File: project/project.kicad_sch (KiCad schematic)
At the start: 26 parts, among them J1 FFC Connector, U1 PCA9555PW, U2 74HC165, U3 ISO1540, U4 GX101, U5 74HC165

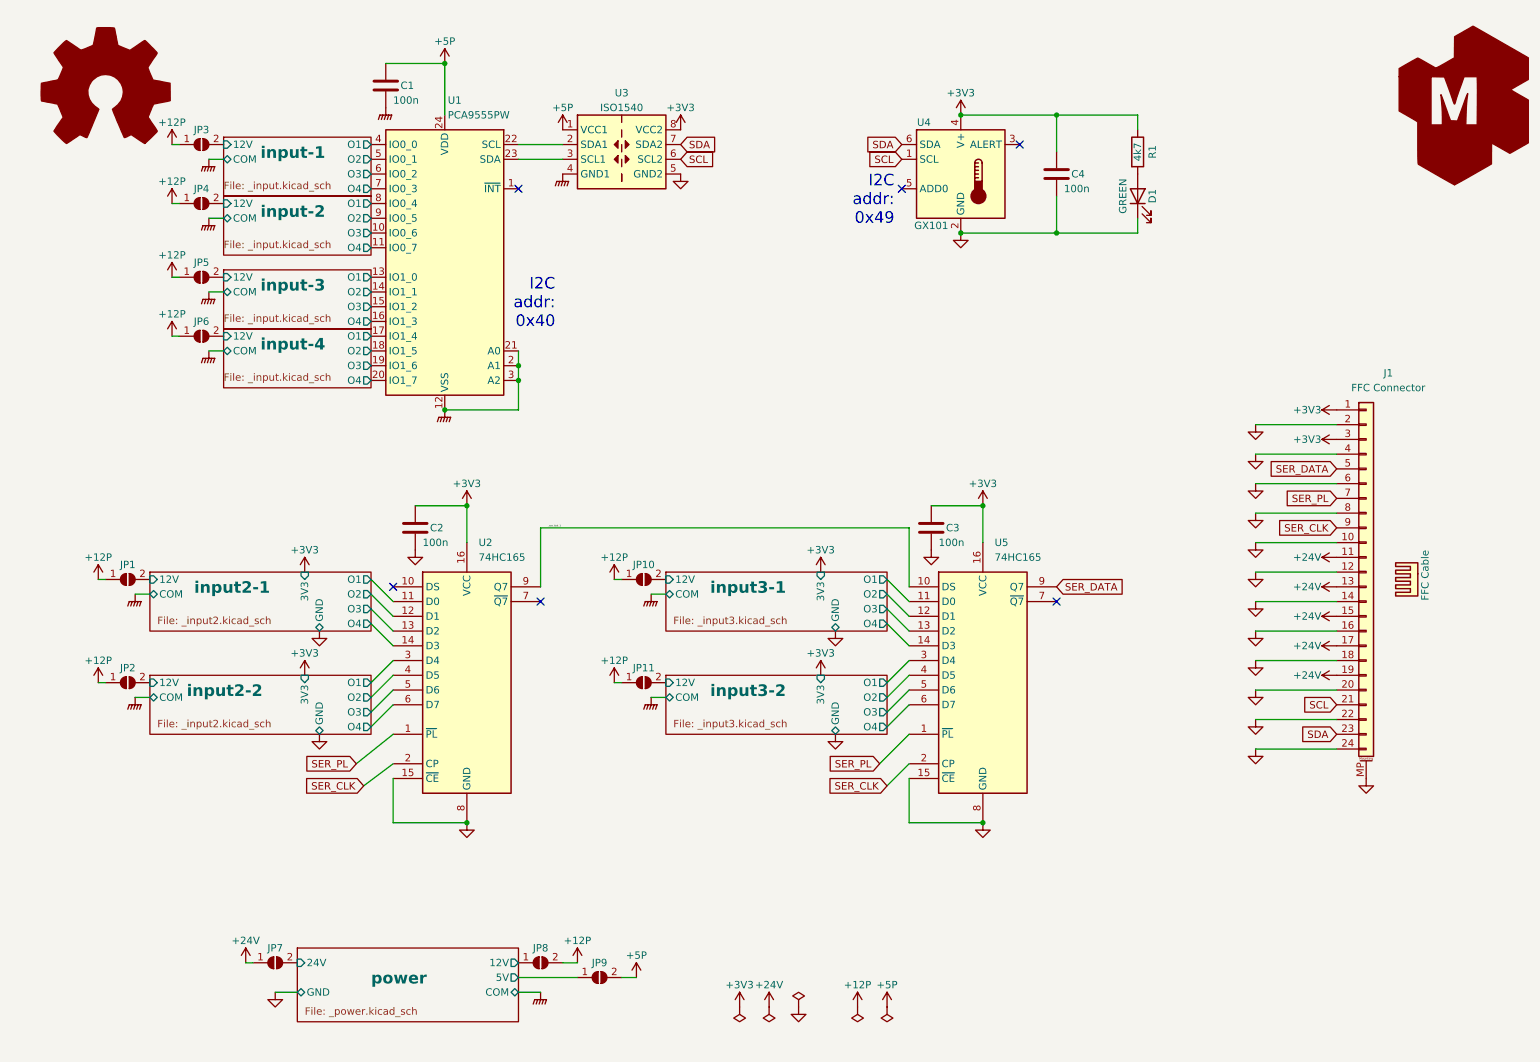
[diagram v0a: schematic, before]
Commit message: refactoring everything to use selected input type
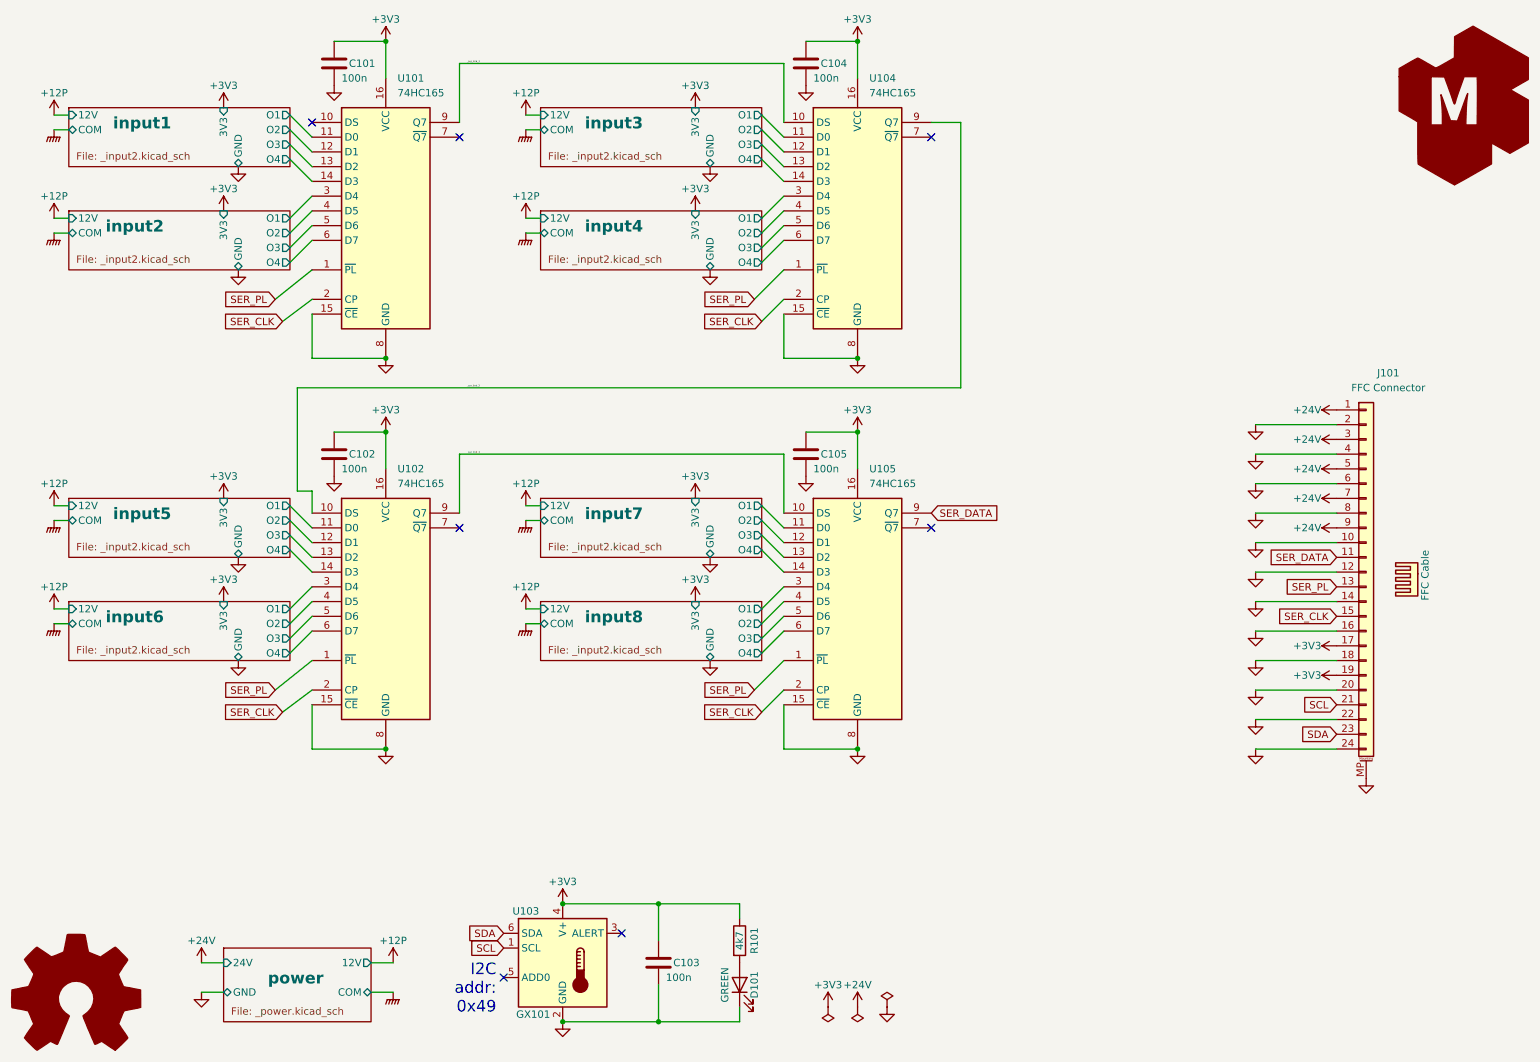
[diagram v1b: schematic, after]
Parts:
- removed C1: 100n, Capacitor_SMD:C_0805_2012Metric_Pad1.18x1.45mm_HandSolder, symbol Device:C
- removed JP1, JP10, JP11, JP2, JP3, JP4, JP5, JP6, JP7, JP8, JP9: SolderJumper_2_Open, Jumper:SolderJumper-2_P1.3mm_Open_TrianglePad1.0x1.5mm, symbol Jumper:SolderJumper_2_Open
- removed U1: PCA9555PW, Package_SO:TSSOP-24_4.4x7.8mm_P0.65mm, symbol Interface_Expansion:PCA9555PW
- removed U3: ISO1540, Package_SO:SOIC-8_3.9x4.9mm_P1.27mm, symbol Isolator:ISO1540
- added C102, C105: 100n, Capacitor_SMD:C_0402_1005Metric_Pad0.74x0.62mm_HandSolder, symbol Device:C
- added U102, U105: 74HC165, Package_SO:TSSOP-16_4.4x5mm_P0.65mm, symbol 74xx:74HC165
- BOM101: renamed from BOM1; jlc-part-type E -> E-wrong
- C101: renamed from C2; footprint Capacitor_SMD:C_0805_2012Metric_Pad1.18x1.45mm_HandSolder -> Capacitor_SMD:C_0402_1005Metric_Pad0.74x0.62mm_HandSolder; lcsc# C28233 -> C307331
- C103: renamed from C4; footprint Capacitor_SMD:C_0805_2012Metric_Pad1.18x1.45mm_HandSolder -> Capacitor_SMD:C_0402_1005Metric_Pad0.74x0.62mm_HandSolder; lcsc# C28233 -> C307331
- C104: renamed from C3; footprint Capacitor_SMD:C_0805_2012Metric_Pad1.18x1.45mm_HandSolder -> Capacitor_SMD:C_0402_1005Metric_Pad0.74x0.62mm_HandSolder; lcsc# C28233 -> C307331
- R101: renamed from R1; lcsc# (none) -> C17673
- renumbered D1 to D101, G1 to G101, G2 to G102, J1 to J101, U2 to U101, U4 to U103, U5 to U104
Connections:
- net +24V: now also J101.1 (Pin_1), J101.3 (Pin_3), J101.5 (Pin_5), J101.7 (Pin_7), J101.9 (Pin_9); no longer J101.11 (Pin_11), J101.13 (Pin_13), J101.15 (Pin_15), J101.17 (Pin_17), J101.19 (Pin_19)
- net +3V3: now also J101.17 (Pin_17), J101.19 (Pin_19), C102.1, C105.1, U102.16 (VCC), U105.16 (VCC); no longer J101.1 (Pin_1), J101.3 (Pin_3)
- net GND: now also C102.2, C105.2, U102.15 (~{CE}), U102.8 (GND), U105.15 (~{CE}), U105.8 (GND)
- net SER_CLK: now also J101.15 (Pin_15), U102.2 (CP), U105.2 (CP); no longer J101.9 (Pin_9)
- net SER_DATA: now also J101.11 (Pin_11), U105.9 (Q7); no longer J101.5 (Pin_5), U104.9 (Q7)
- net SER_PL: now also J101.13 (Pin_13), U102.1 (~{PL}), U105.1 (~{PL}); no longer J101.7 (Pin_7)
- net _ser_link_1: now also U102.9 (Q7), U105.10 (DS); no longer U101.9 (Q7), U104.10 (DS)
- net input3-1/O1 renamed input3/O1
- net input3-1/O2 renamed input3/O2
- net input3-1/O3 renamed input3/O3
- net input3-1/O4 renamed input3/O4
- net input3-2/O1 renamed input4/O1
- net input3-2/O2 renamed input4/O2
- net input3-2/O3 renamed input4/O3
- net input3-2/O4 renamed input4/O4
- new net _ser_link_2: U102.10 (DS), U104.9 (Q7)
- new net _ser_link_3: U101.9 (Q7), U104.10 (DS)
- new net input5/O1: U102.11 (D0)
- new net input5/O2: U102.12 (D1)
- new net input5/O3: U102.13 (D2)
- new net input5/O4: U102.14 (D3)
- new net input6/O1: U102.3 (D4)
- new net input6/O2: U102.4 (D5)
- new net input6/O3: U102.5 (D6)
- new net input6/O4: U102.6 (D7)
- new net input7/O1: U105.11 (D0)
- new net input7/O2: U105.12 (D1)
- new net input7/O3: U105.13 (D2)
- new net input7/O4: U105.14 (D3)
- new net input8/O1: U105.3 (D4)
- new net input8/O2: U105.4 (D5)
- new net input8/O3: U105.5 (D6)
- new net input8/O4: U105.6 (D7)
- no-connect marks 6 -> 7
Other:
- sheet input2-1 renamed input1
- sheet input2-2 renamed input2
- removed sheet input-1
- removed sheet input-2
- removed sheet input-3
- removed sheet input-4
- removed sheet input3-1
- removed sheet input3-2
- added sheet input3 (_input2.kicad_sch)
- added sheet input4 (_input2.kicad_sch)
- added sheet input5 (_input2.kicad_sch)
- added sheet input6 (_input2.kicad_sch)
- added sheet input7 (_input2.kicad_sch)
- added sheet input8 (_input2.kicad_sch)
- sheet power ports: added none; removed 5V
- note removed: "I2C addr: 0x40"
- moved on the sheet: C101, C103, C104, D101, R101, U101, U103, U104

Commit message: replacing thermometer
* Switching to TMP102 as TMP101 is no longer available
* bumping up version
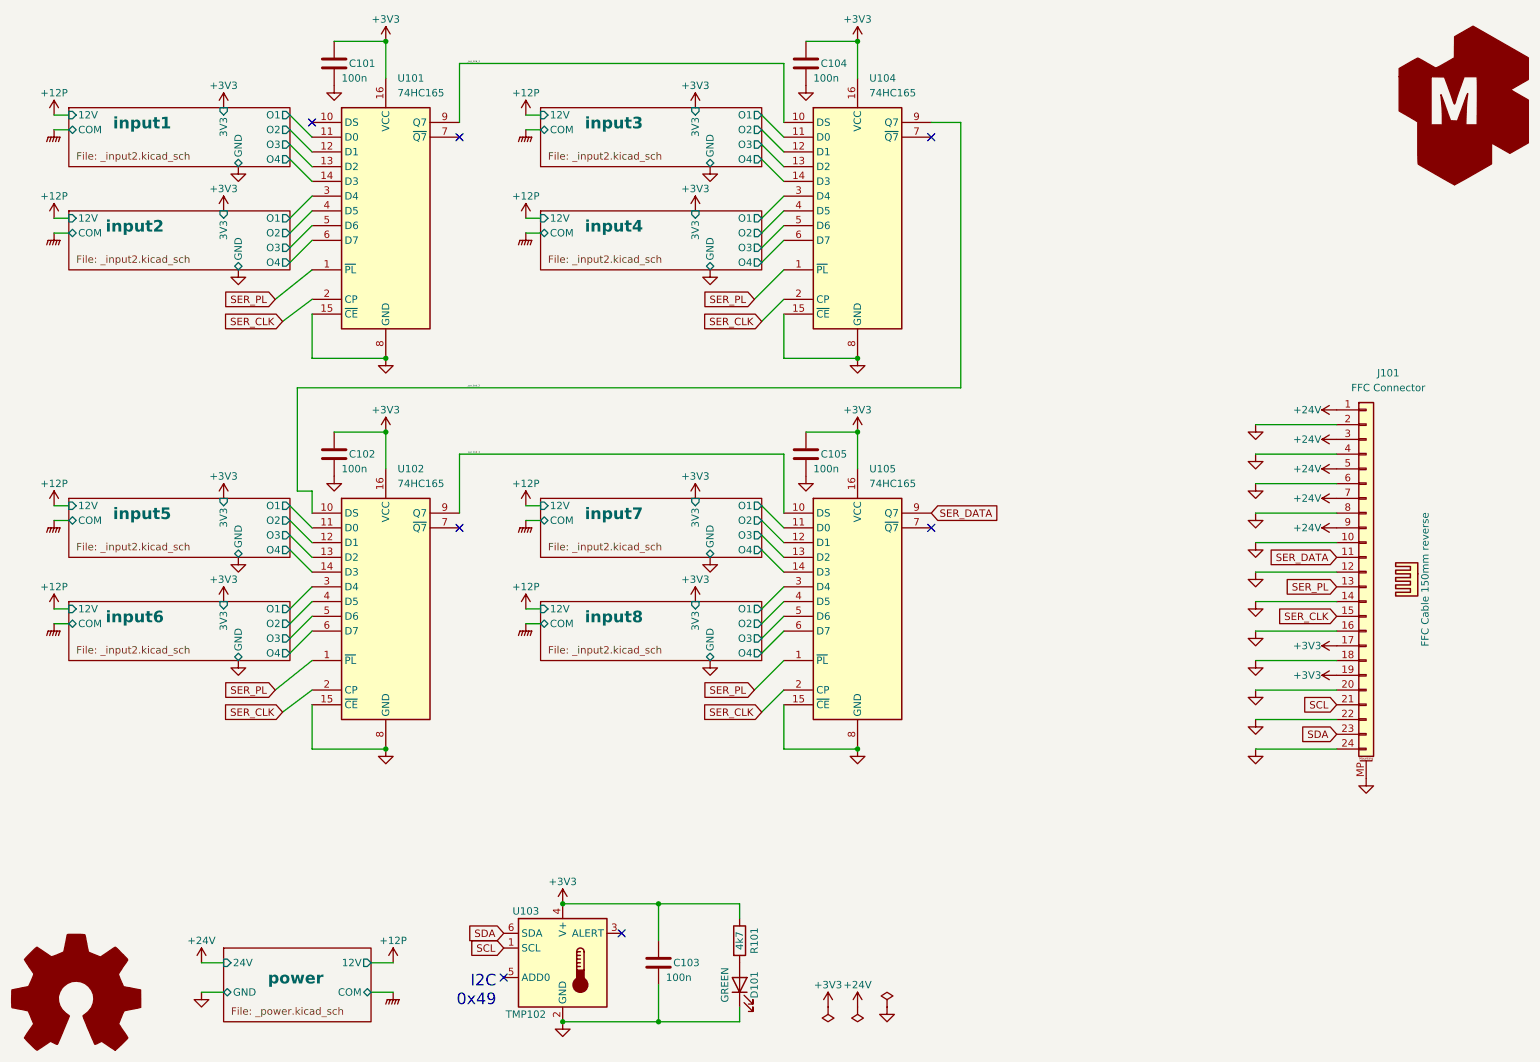
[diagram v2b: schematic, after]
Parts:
- BOM101: value FFC Cable -> FFC Cable 150mm reverse; jlc-part-type E-wrong -> E; lcsc# C20616071 -> C42434316
- U103: value GX101 -> TMP102; footprint Package_TO_SOT_SMD:SOT-23-6 -> -local:SOT-563; lcsc# C5441728 -> C99269
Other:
- note added: "I2C 0x49"
- note removed: "I2C addr: 0x49"
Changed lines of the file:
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@@
   (title_block
     (title "WormControl-Input32-InputBoard")
-    (date "2026-01-29")
-    (rev "0.2")
+    (date "2026-03-19")
+    (rev "0.3")
     (company "makerspace.lt")
   )
@@
     (stroke (width 0) (type default) (color 0 0 0 0))
   )
-  (text "I2C\naddr:\n0x49" (at 97.79 189.23 180)
+  (text "I2C\n0x49" (at 97.79 187.96 180)
     (effects (font (size 2 2)) (justify right bottom))
   )
@@
     (in_bom yes) (on_board yes)
     (property "Reference" "U103" (id 0) (at 102.87 171.45 0))
-    (property "Value" "GX101" (id 1) (at 104.14 189.23 0))
-    (property "Footprint" "Package_TO_SOT_SMD:SOT-23-6" (id 2) (at 110.49 189.23 0)
+    (property "Value" "TMP102" (id 1) (at 102.87 189.23 0))
+    (property "Footprint" "-local:SOT-563" (id 2) (at 110.49 189.23 0)
       (effects (font (size 1.27 1.27)) (justify left) hide)
     )
-    (property "Datasheet" "https://www.ti.com/lit/ds/symlink/tmp101.pdf" (id 3) (at 110.49 191.77 0)
+    (property "Datasheet" "https://www.lcsc.com/datasheet/C99269.pdf" (id 3) (at 110.49 191.77 0)
       (effects (font (size 1.27 1.27)) (justify left) hide)
     )
@@
       (effects (font (size 1.27 1.27)) hide)
     )
-    (property "lcsc#" "C5441728" (id 5) (at 109.22 180.34 0)
+    (property "lcsc#" "C99269" (id 5) (at 109.22 180.34 0)
       (effects (font (size 1.27 1.27)) hide)
     )
@@
       (effects (font (size 1.27 1.27)) (justify left) hide)
     )
-    (property "Value" "FFC Cable" (id 1) (at 257.81 109.22 0)
-      (effects (font (size 1.27 1.27)) (justify left))
-    )
+    (property "Value" "FFC Cable 150mm reverse" (id 1) (at 257.81 114.3 0))
     (property "Footprint" "" (id 2) (at 256.54 114.6048 0)
       (effects (font (size 1.27 1.27)) hide)
     )
-    (property "Datasheet" "~" (id 3) (at 256.54 114.6048 0)
+    (property "Datasheet" "https://www.lcsc.com/datasheet/C42434316.pdf" (id 3) (at 256.54 114.6048 0)
       (effects (font (size 1.27 1.27)) hide)
     )
-    (property "lcsc#" "C20616071" (id 4) (at 256.54 114.3 0)
+    (property "lcsc#" "C42434316" (id 4) (at 256.54 114.3 0)
       (effects (font (size 1.27 1.27)) hide)
     )
-    (property "jlc-part-type" "E-wrong" (id 5) (at 256.54 114.3 0)
+    (property "jlc-part-type" "E" (id 5) (at 256.54 114.3 0)
       (effects (font (size 1.27 1.27)) hide)
     )
@@
     )
     (path "/854d2a9d-cac9-4835-b3ce-fd1841d04aca"
-      (reference "BOM101") (unit 1) (value "FFC Cable") (footprint "")
+      (reference "BOM101") (unit 1) (value "FFC Cable 150mm reverse") (footprint "")
     )
     (path "/90e4b13a-cd4c-4d9b-8f76-177c78aec094/3eeff65a-5b97-4673-8b7f-10417da95f23"
@@
     )
     (path "/55cbd1b5-ecb1-4b1b-9a94-3461217e0d3f"
-      (reference "U103") (unit 1) (value "GX101") (footprint "Package_TO_SOT_SMD:SOT-23-6")
+      (reference "U103") (unit 1) (value "TMP102") (footprint "-local:SOT-563")
     )
     (path "/8332810e-c1e4-419d-9847-410e424bf1c5"

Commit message: fixing tmp102 pinout
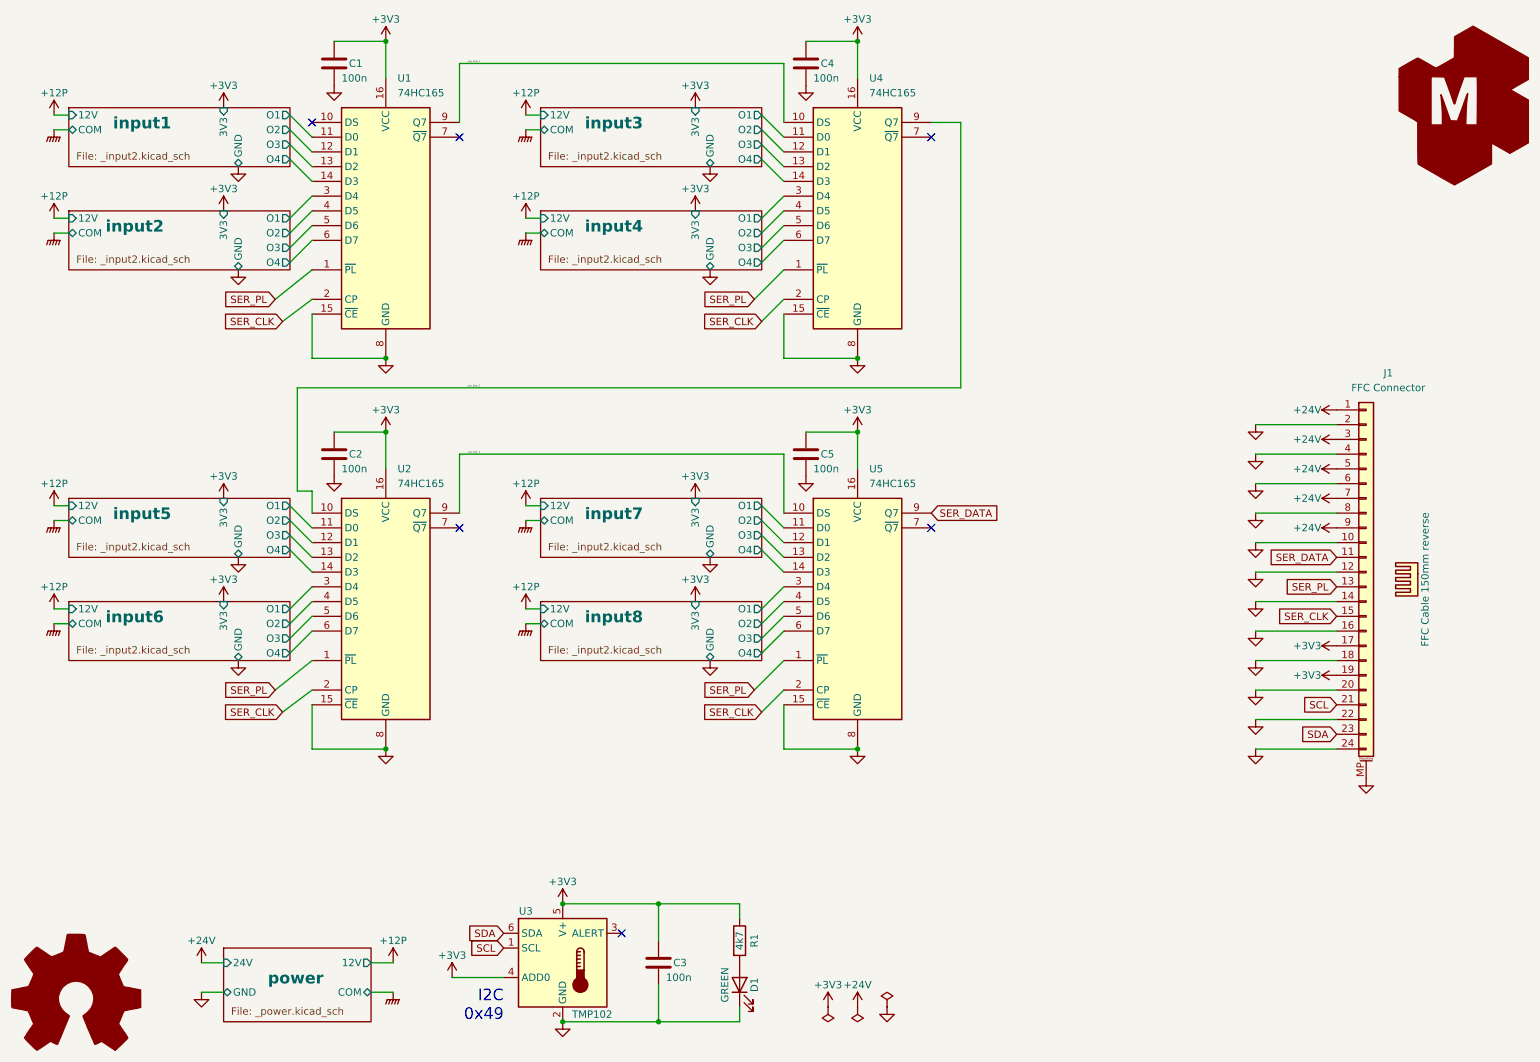
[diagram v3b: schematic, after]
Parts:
- U3: renamed from U103; symbol Sensor_Temperature:TMP101 -> Sensor_Temperature:TMP102xxDRL
- renumbered BOM101 to BOM1, C101 to C1, C102 to C2, C103 to C3, C104 to C4, C105 to C5, D101 to D1, G101 to G1, G102 to G2, J101 to J1, R101 to R1, U101 to U1, U102 to U2, U104 to U4, U105 to U5
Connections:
- net +3V3: now also U3.5 (V+)
- no-connect marks 7 -> 6
